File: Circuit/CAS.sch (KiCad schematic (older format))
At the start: 32 parts, among them IC1 ATTINY13A-P, P1 USB_B, P2 CONN_01X03, P3 CONN_01X03, P4 CONN_01X02, P5 CONN_01X03, P6 USB_B, P7 CONN_01X03, Q1 2N2222, Q2 2N3906, Q3 2N2222, U1 MICRO-B_USB, U2 PC817, U3 MICRO-B_USB

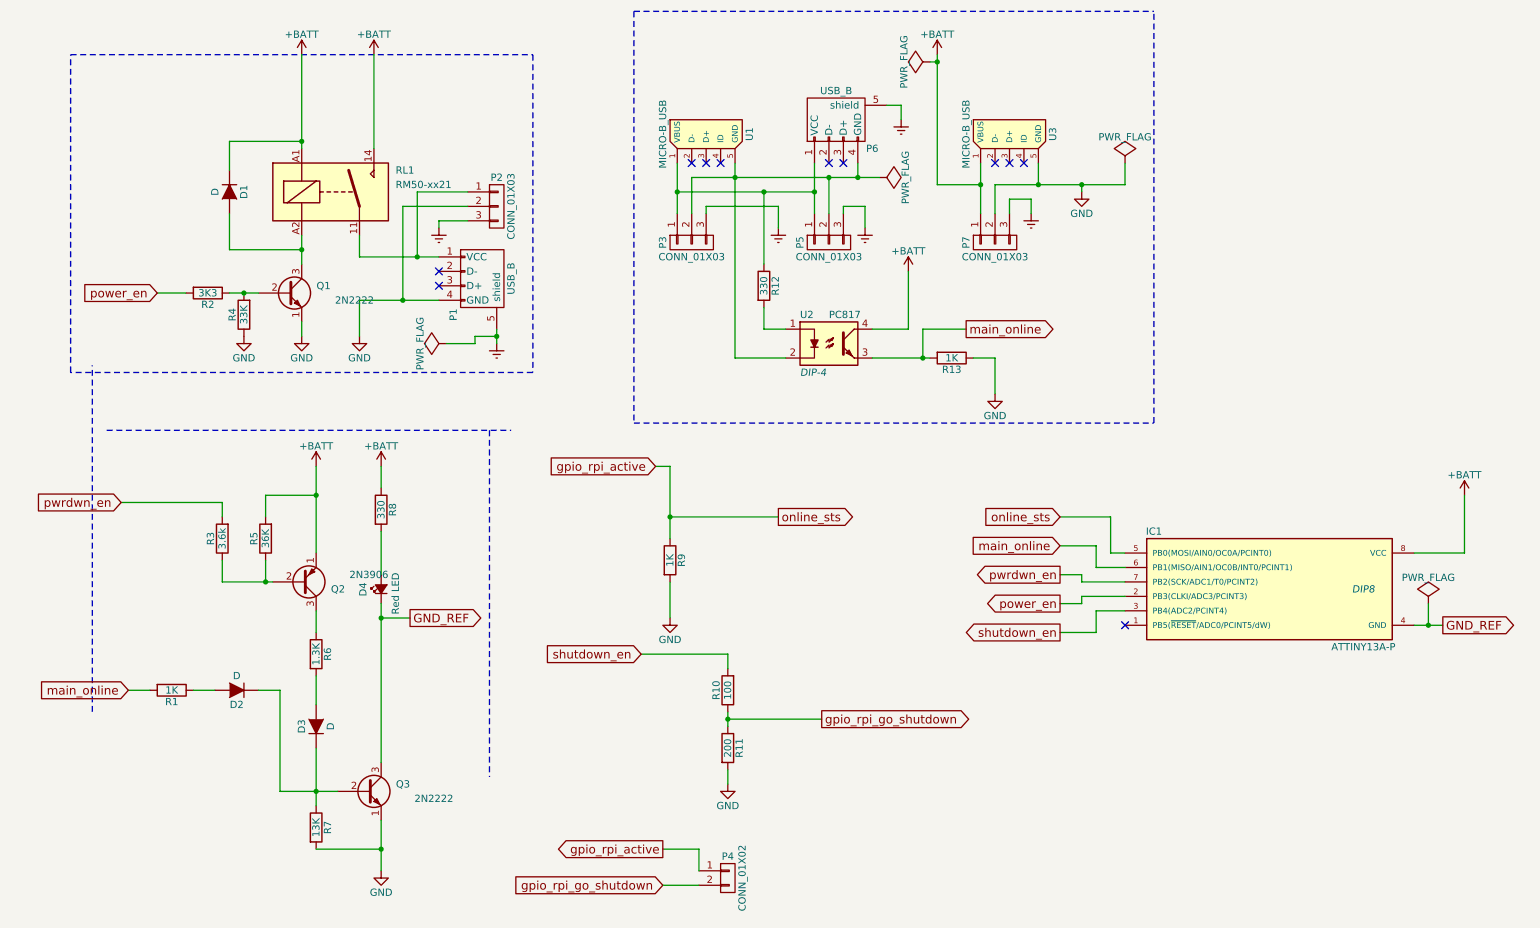
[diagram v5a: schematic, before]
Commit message: Revise schematic to multi-level schematic
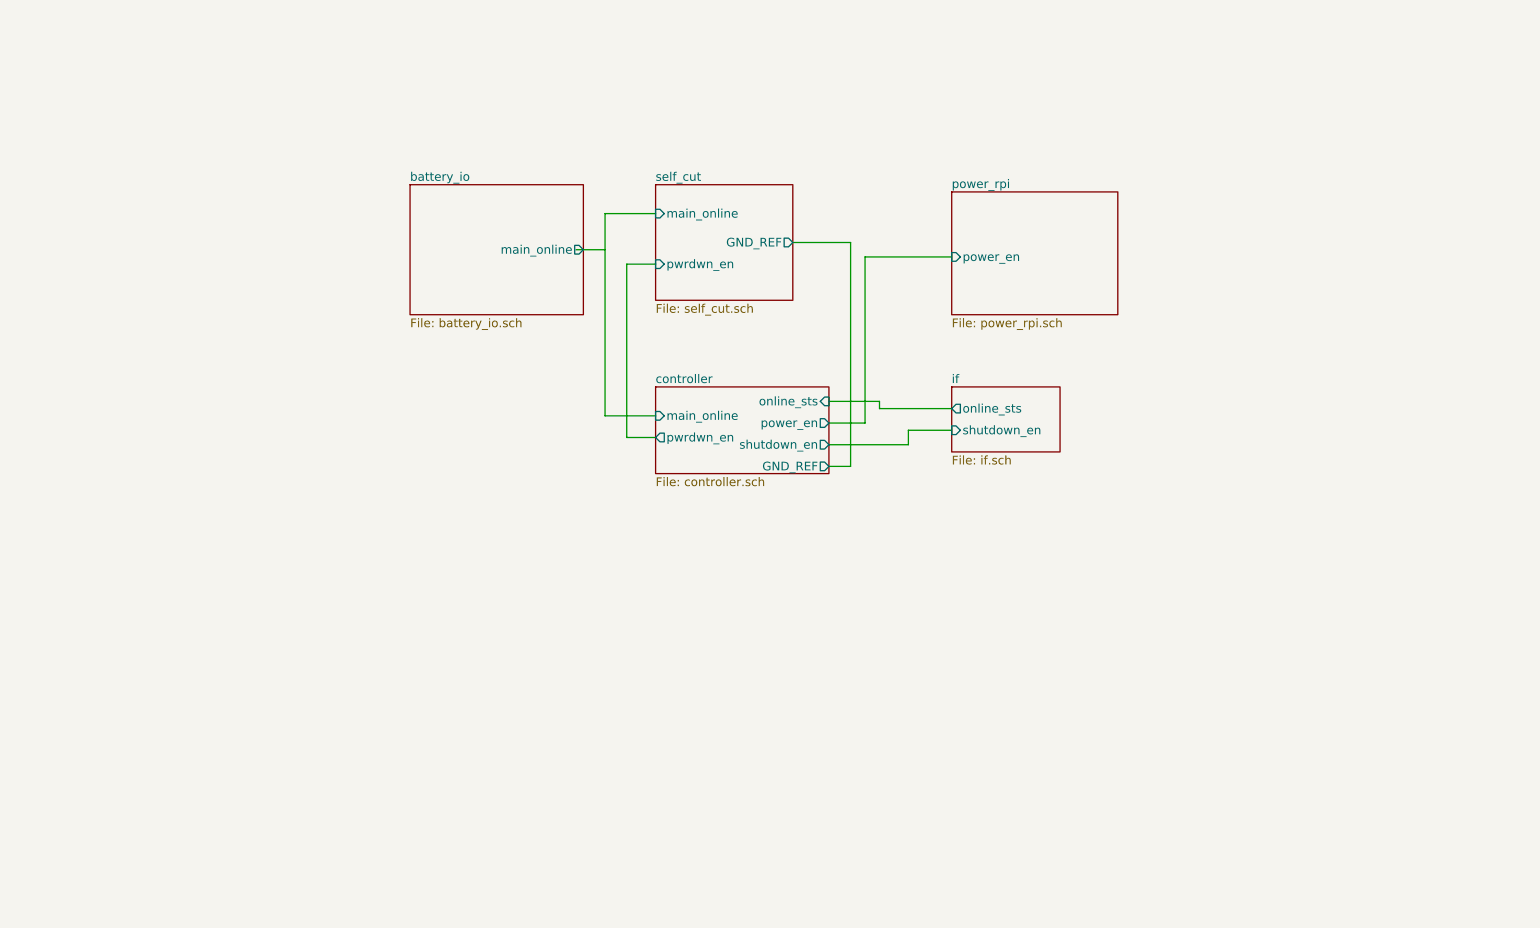
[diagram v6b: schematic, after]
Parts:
- removed D1, D2, D3: D, symbol D
- removed D4: Red LED, symbol Led_Small
- removed IC1: ATTINY13A-P, DIP8, symbol ATTINY13A-P
- removed P1, P6: USB_B, symbol USB_B
- removed P2, P3, P5, P7: CONN_01X03, symbol CONN_01X03
- removed P4: CONN_01X02, symbol CONN_01X02
- removed Q1, Q3: 2N2222, symbol Q_NPN_EBC
- removed Q2: 2N3906, symbol Q_PNP_EBC
- removed R1, R13, R9: 1K, symbol R
- removed R10: 100, symbol R
- removed R11: 200, symbol R
- removed R12, R8: 330, symbol R
- removed R2: 3K3, symbol R
- removed R3: 3.6k, symbol R
- removed R4: 33K, symbol R
- removed R5: 36K, symbol R
- removed R6: 1.3K, symbol R
- removed R7: 13K, symbol R
- removed RL1: RM50-xx21, symbol RM50-xx21
- removed U1, U3: MICRO-B_USB, symbol MICRO-B_USB
- removed U2: PC817, DIP-4, symbol PC817
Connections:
- net labels removed: +BATT, Earth, GND, GND_REF, gpio_rpi_active, gpio_rpi_go_shutdown, main_online, online_sts, power_en, pwrdwn_en, shutdown_en
- wire segments 116 -> 19
- no-connect marks 11 -> 0
